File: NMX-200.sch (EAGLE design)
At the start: 93 parts, among them IC1 AT90USB1287-AU, IC2 AT90USB1287-MU, J1 PJ-002AH, J2 10118193-0001LF, J3 SJ1-2503A, J4 RJHSE-5385-02, J5 SJ1-2503A, J6 SJ1-2503A, Q1 P-CHANNEL_MOSFET, T1 CMPT2369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

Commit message: Updated TVS Attributes
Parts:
- U16, U17, U18, U8: MF (none) -> Bourns Inc; MPN (none) -> SMAJ48CA
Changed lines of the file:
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@@
 <part name="U$3" library="adafruit" deviceset="FIDUCIAL" device=""/>
 <part name="U$4" library="adafruit" deviceset="FIDUCIAL" device=""/>
-<part name="U8" library="QS_Components" deviceset="TVS_SMA" device=""/>
-<part name="U16" library="QS_Components" deviceset="TVS_SMA" device=""/>
-<part name="U17" library="QS_Components" deviceset="TVS_SMA" device=""/>
-<part name="U18" library="QS_Components" deviceset="TVS_SMA" device=""/>
+<part name="U8" library="QS_Components" deviceset="TVS_SMA" device="">
+<attribute name="MF" value="Bourns Inc"/>
+<attribute name="MPN" value="SMAJ48CA"/>
+</part>
+<part name="U16" library="QS_Components" deviceset="TVS_SMA" device="">
+<attribute name="MF" value="Bourns Inc"/>
+<attribute name="MPN" value="SMAJ48CA"/>
+</part>
+<part name="U17" library="QS_Components" deviceset="TVS_SMA" device="">
+<attribute name="MF" value="Bourns Inc"/>
+<attribute name="MPN" value="SMAJ48CA"/>
+</part>
+<part name="U18" library="QS_Components" deviceset="TVS_SMA" device="">
+<attribute name="MF" value="Bourns Inc"/>
+<attribute name="MPN" value="SMAJ48CA"/>
+</part>
 </parts>
 <sheets>
@@
 <instance part="U$3" gate="G$1" x="193.04" y="175.26"/>
 <instance part="U$4" gate="G$1" x="193.04" y="167.64"/>
-<instance part="U8" gate="G$1" x="93.98" y="215.9" rot="R90"/>
-<instance part="U16" gate="G$1" x="104.14" y="215.9" rot="R90"/>
-<instance part="U17" gate="G$1" x="114.3" y="215.9" rot="R90"/>
-<instance part="U18" gate="G$1" x="124.46" y="215.9" rot="R90"/>
+<instance part="U8" gate="G$1" x="93.98" y="215.9" rot="R90">
+<attribute name="MF" x="93.98" y="215.9" size="1.778" layer="96" rot="R90" display="off"/>
+<attribute name="MPN" x="93.98" y="215.9" size="1.778" layer="96" rot="R90" display="off"/>
+</instance>
+<instance part="U16" gate="G$1" x="104.14" y="215.9" rot="R90">
+<attribute name="MF" x="104.14" y="215.9" size="1.778" layer="96" rot="R90" display="off"/>
+<attribute name="MPN" x="104.14" y="215.9" size="1.778" layer="96" rot="R90" display="off"/>
+</instance>
+<instance part="U17" gate="G$1" x="114.3" y="215.9" rot="R90">
+<attribute name="MF" x="114.3" y="215.9" size="1.778" layer="96" rot="R90" display="off"/>
+<attribute name="MPN" x="114.3" y="215.9" size="1.778" layer="96" rot="R90" display="off"/>
+</instance>
+<instance part="U18" gate="G$1" x="124.46" y="215.9" rot="R90">
+<attribute name="MF" x="124.46" y="215.9" size="1.778" layer="96" rot="R90" display="off"/>
+<attribute name="MPN" x="124.46" y="215.9" size="1.778" layer="96" rot="R90" display="off"/>
+</instance>
 </instances>
 <busses>

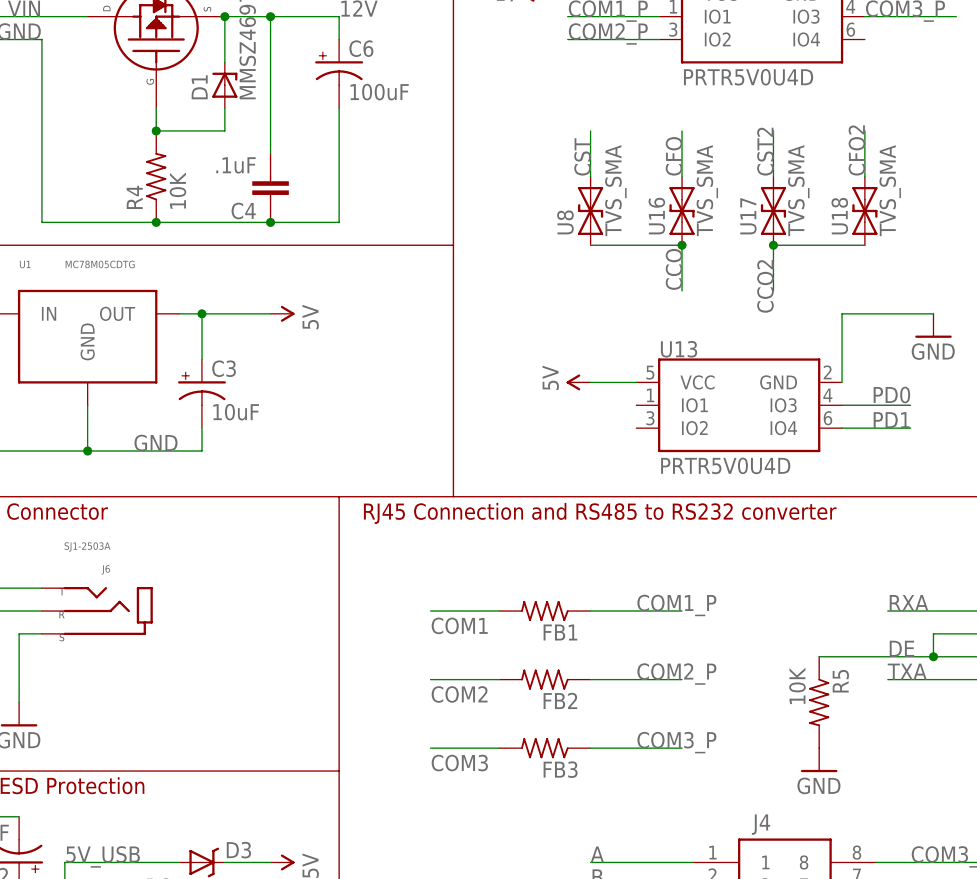
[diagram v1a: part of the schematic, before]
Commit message: Fixed NMX-200 schematic typo
Two 10k resistors were marked with an upper case "K" instead of lower
case k", which caused them to appear as a separate line on the exported
BOM.
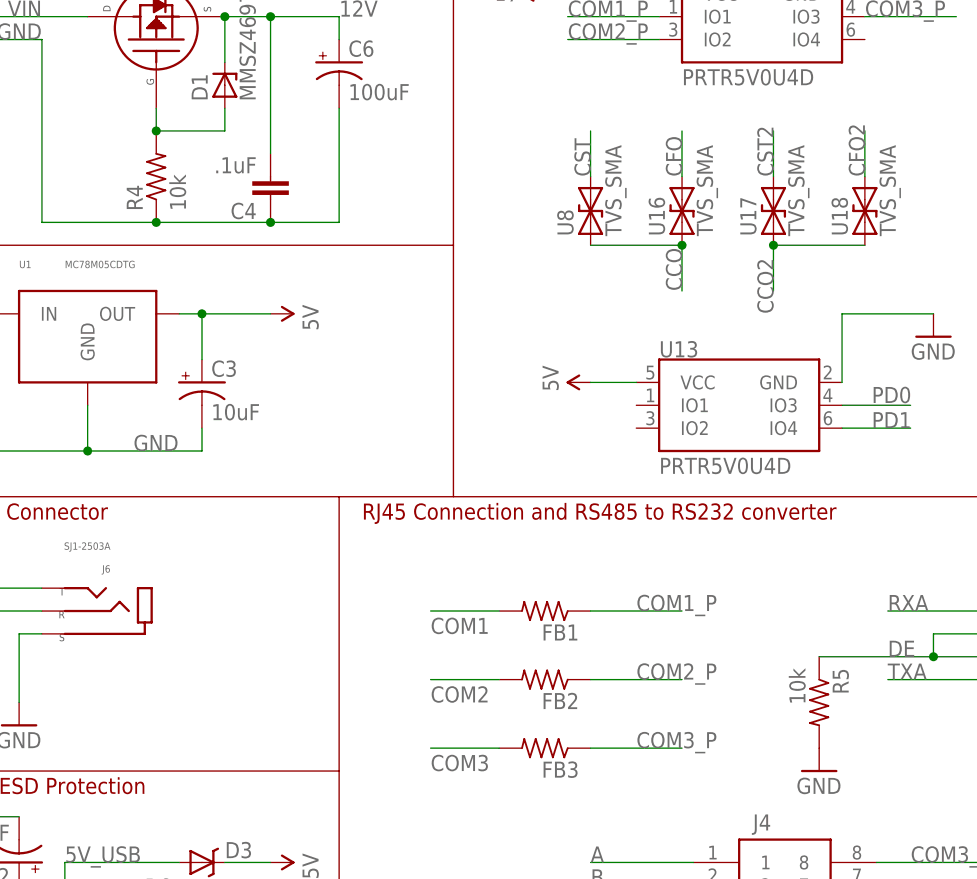
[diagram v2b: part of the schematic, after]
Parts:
- R4, R5: value 10K -> 10k
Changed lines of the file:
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@@
 <?xml version="1.0" encoding="utf-8"?>
 <!DOCTYPE eagle SYSTEM "eagle.dtd">
-<eagle version="6.6.0">
+<eagle version="6.5.0">
 <drawing>
 <settings>
@@
 <attribute name="MPN" value="FDS6681Z"/>
 </part>
-<part name="R4" library="resistor" deviceset="R-US_" device="R0402" value="10K">
+<part name="R4" library="resistor" deviceset="R-US_" device="R0402" value="10k">
 <attribute name="MF" value="Yageo"/>
 <attribute name="MPN" value="RC0402FR-0710KL"/>
@@
 <attribute name="MPN" value="RC0402JR-07120RL"/>
 </part>
-<part name="R5" library="resistor" deviceset="R-US_" device="R0402" value="10K">
+<part name="R5" library="resistor" deviceset="R-US_" device="R0402" value="10k">
 <attribute name="MF" value="Yageo"/>
 <attribute name="MPN" value="RC0402FR-0710KL"/>

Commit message: Changed silkscreen to indicate polarity of some components
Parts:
- D2: device NMX_ControllerSide_v1-3:ZENER-DIODESOD123 -> diode:ZENER-DIODESOD123
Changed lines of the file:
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@@
 <?xml version="1.0" encoding="utf-8"?>
 <!DOCTYPE eagle SYSTEM "eagle.dtd">
-<eagle version="6.5.0">
+<eagle version="6.6.0">
 <drawing>
 <settings>
@@
 <attribute name="MPN" value="RC0402JR-0722RL"/>
 </part>
-<part name="D2" library="NMX_ControllerSide_v1-3" deviceset="ZENER-DIODE" device="SOD123" value="MMSZ5253B">
+<part name="D2" library="diode" deviceset="ZENER-DIODE" device="SOD123" value="MMSZ5253B">
 <attribute name="MF" value="Fairchild Semiconductor"/>
 <attribute name="MPN" value="MMSZ5253B"/>
